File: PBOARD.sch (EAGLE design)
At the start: 11 parts, among them J1 POWER_JACKPTH_SLOTS, J10 POWER_JACKPTH_SLOTS, J2 POWER_JACKPTH_SLOTS, J3 POWER_JACKPTH_SLOTS, J4 POWER_JACKPTH_SLOTS, J5 POWER_JACKPTH_SLOTS, J7 POWER_JACKPTH_SLOTS, J8 POWER_JACKPTH_SLOTS, J9 POWER_JACKPTH_SLOTS

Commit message: Merged files from PowerDistributionBoard project
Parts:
- removed J10: POWER_JACKPTH_SLOTS, freetronics-jon:POWER_JACKPTH_SLOTS
- removed LED1: GREEN, freetronics-jon:LED3MM
- removed R1: 1K, freetronics-jon:RESISTORPTH1
- added J6: POWER_JACKPTH_SLOTS, freetronics-jon:POWER_JACKPTH_SLOTS
- added JP1: (no value), freetronics-jon:M025MM
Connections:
- removed net 3.3V: J1.PWR, J10.PWR, J2.PWR, J3.PWR, J4.PWR, J5.PWR, J7.PWR, J8.PWR, J9.PWR, R1.1
- removed net N$1: LED1.A, R1.2
- new net VCC: J1.PWR, J2.PWR, J3.PWR, J4.PWR, J5.PWR, J6.PWR, J7.PWR, J8.PWR, J9.PWR, JP1.2
- net GND: now also J6.GND, J6.GNDBREAK, JP1.1; no longer J10.GND, J10.GNDBREAK, LED1.C
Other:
- note added: "Project template for OODTY case"
- note added: "Released under the TAPR Open Hardware License: tapr.org/OHL"
- note added: "V1.0 (2018-10-16)"
- note added: "www.superhouse.tv"
- note removed: "(C) 2018 Freetronics Pty Ltd"
- note removed: "Power Breakout Board"
- note removed: "Released under the TAPR Open Hardware License: tapr.org/ohl"
- note removed: "SKU: PBOARD"
- note removed: "V1.0 (2018-09-30)"
- note removed: "www.freetronics.com.au/pboard"
- moved on the sheet: J1, J2, J3, J4, J5, J7, J8, J9

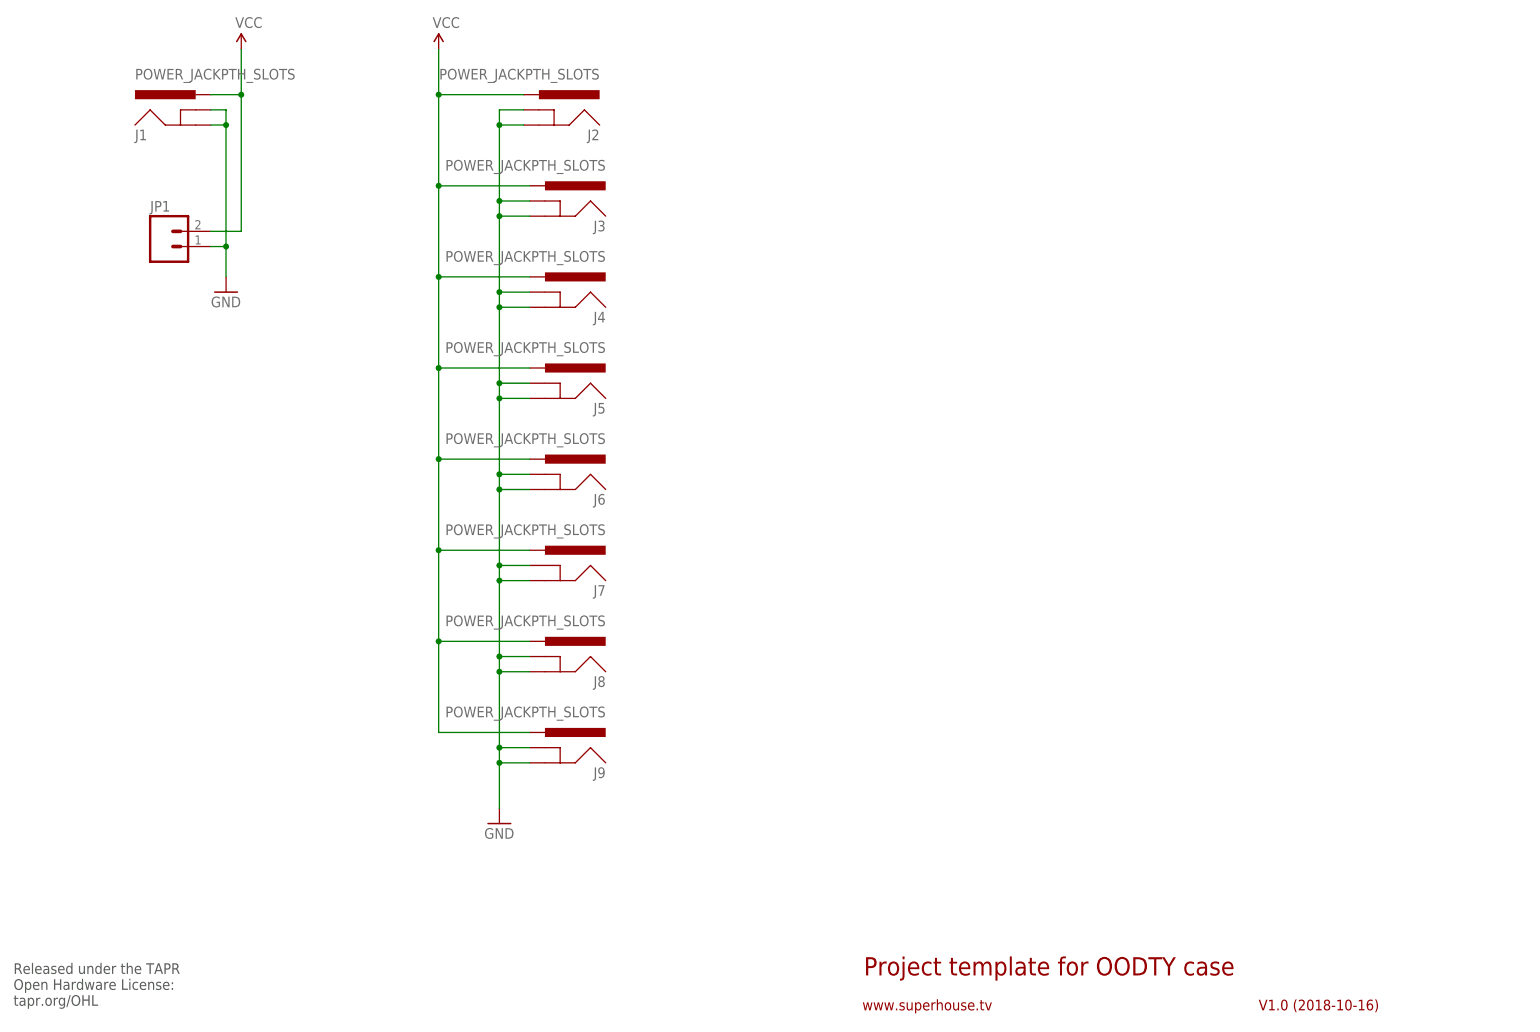
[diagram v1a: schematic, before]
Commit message: Added power LED for v1.0 release
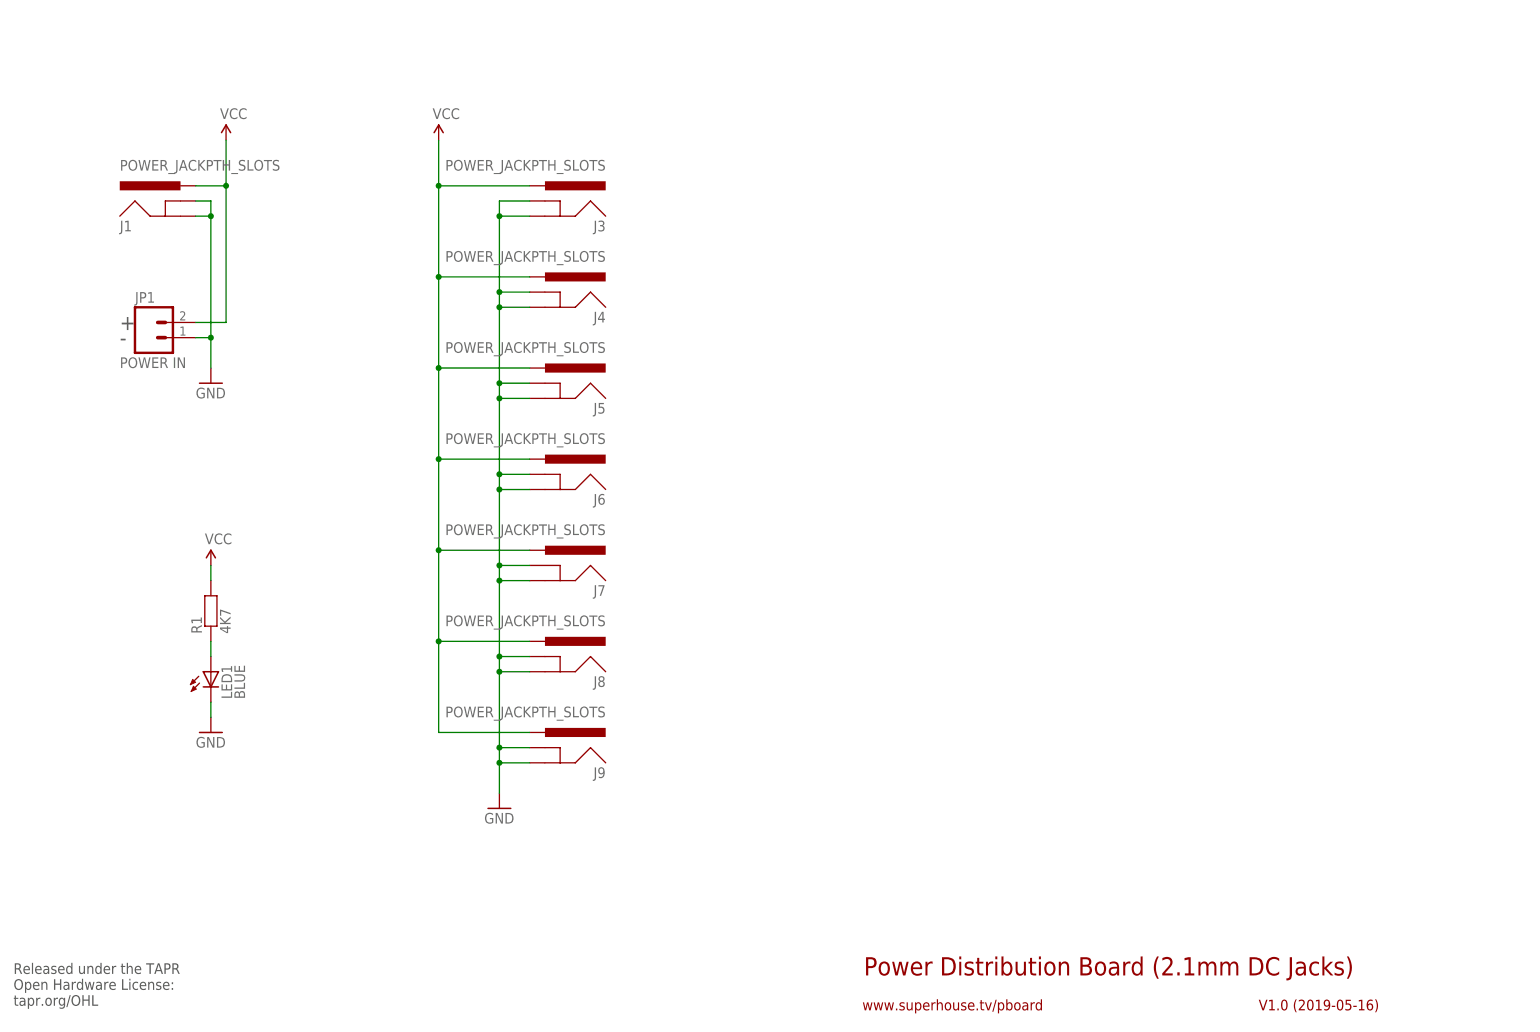
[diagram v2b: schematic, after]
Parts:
- removed J2: POWER_JACKPTH_SLOTS, freetronics-jon:POWER_JACKPTH_SLOTS
- added LED1: BLUE, freetronics-jon:LED3MM
- added R1: 4K7, freetronics-jon:RESISTORPTH1
- JP1: value (none) -> POWER IN
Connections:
- new net N$1: LED1.A, R1.1
- net GND: now also LED1.C; no longer J2.GND, J2.GNDBREAK
- net VCC: now also R1.2; no longer J2.PWR
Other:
- note added: "+"
- note added: "-"
- note added: "Power Distribution Board (2.1mm DC Jacks)"
- note added: "V1.0 (2019-05-16)"
- note added: "www.superhouse.tv/pboard"
- note removed: "Project template for OODTY case"
- note removed: "V1.0 (2018-10-16)"
- note removed: "www.superhouse.tv"
- moved on the sheet: J1, JP1
